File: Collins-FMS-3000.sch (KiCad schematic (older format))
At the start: 24 parts, among them U2 MCP23017_SO, U3 MCP23017_SO, U4 IS31FL3733B

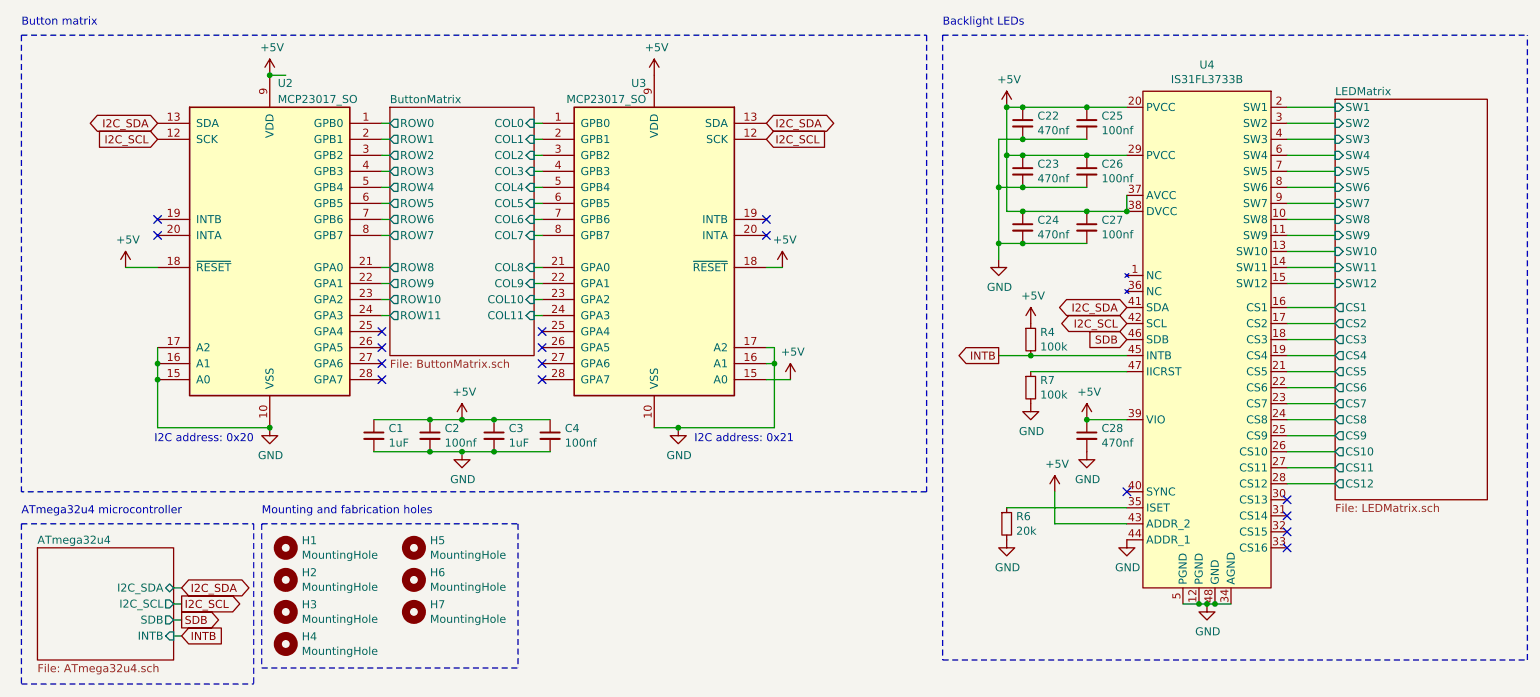
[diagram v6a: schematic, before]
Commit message: Remove diodes, update interrupt connections
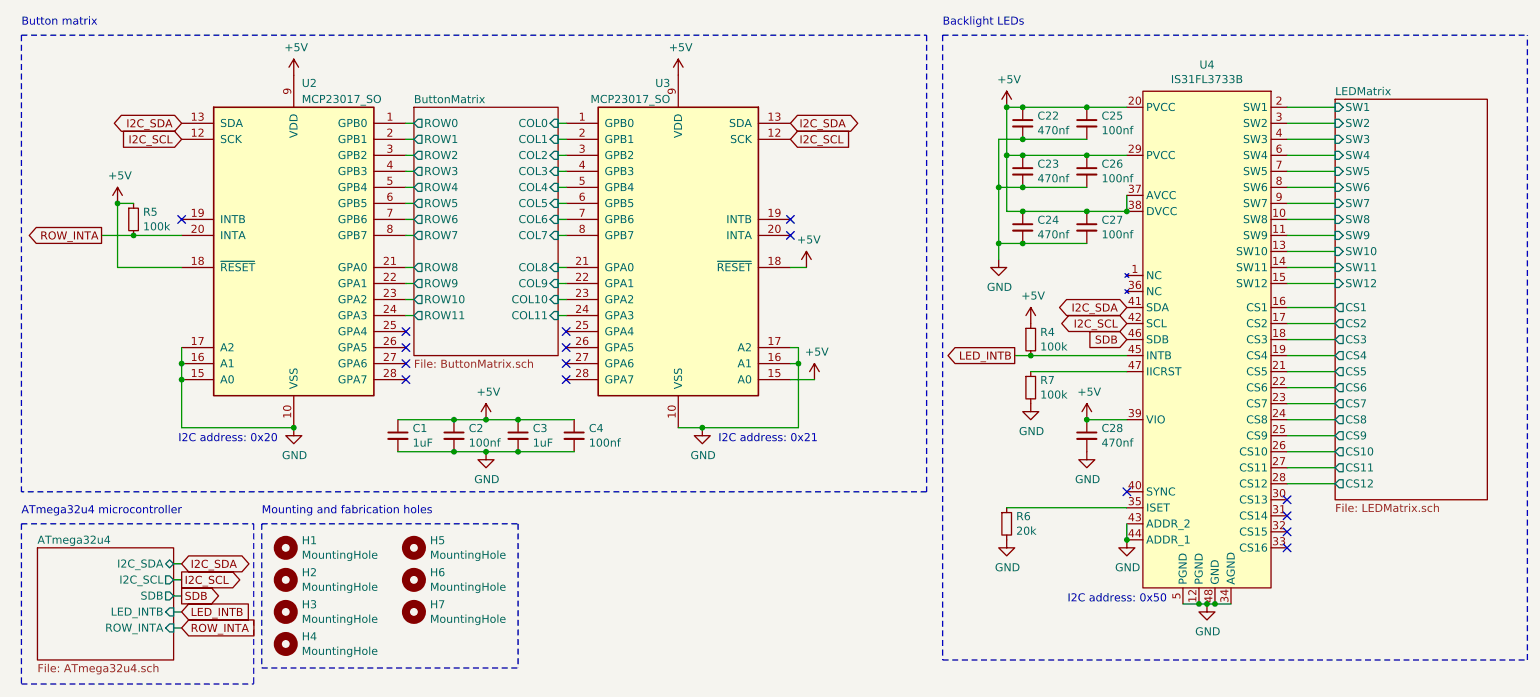
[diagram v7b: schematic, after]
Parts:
- added R5: 100k, Resistor_SMD:R_0402_1005Metric, symbol Device:R_Small
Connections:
- net +5V: now also R5.1; no longer U4.43 (ADDR_2)
- net GND: now also U4.43 (ADDR_2)
- net ROW_INTA: now reaches U2.20 (INTA)
- net ROW_INTA: now also R5.2
- net INTB renamed LED_INTB
- no-connect marks 17 -> 16
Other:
- note added: "I2C address: 0x50"
- moved on the sheet: C1, C2, C3, C4, U2, U3

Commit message: Connect unused pins
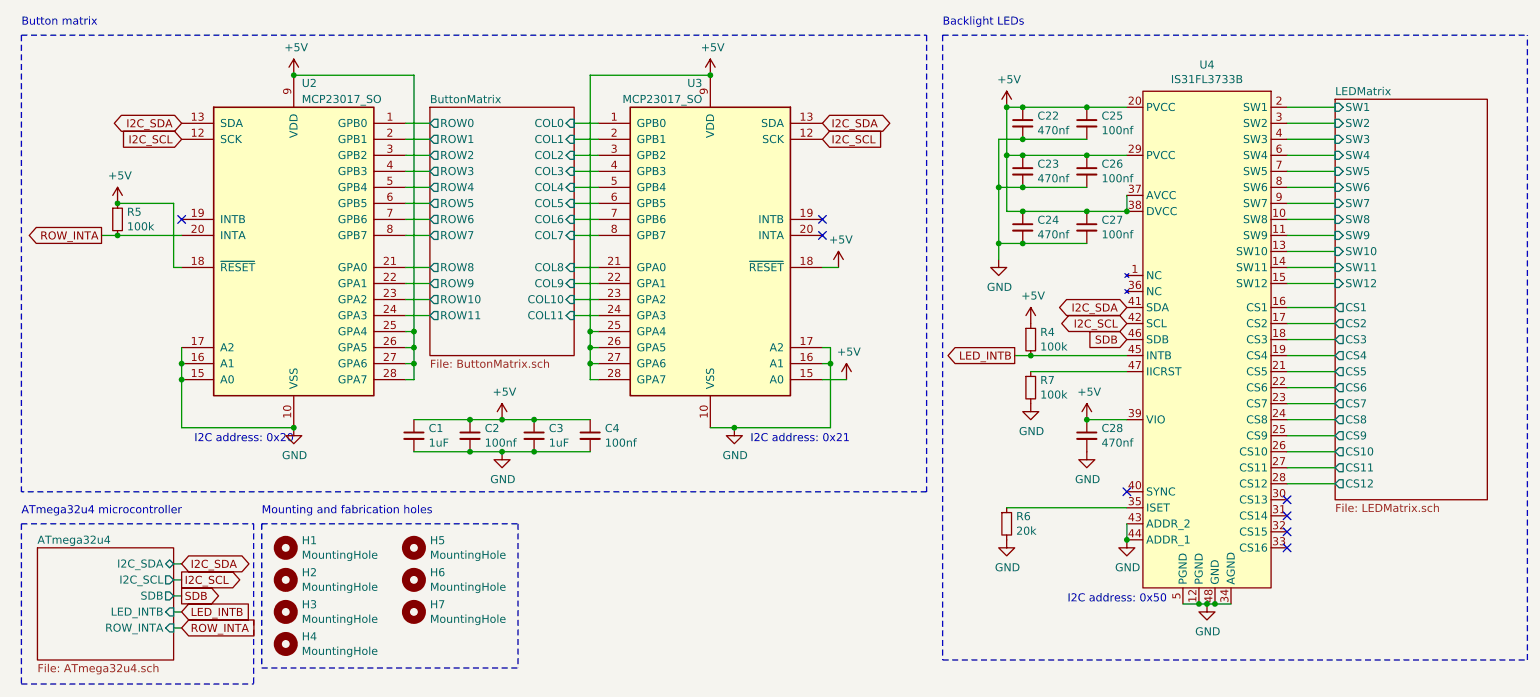
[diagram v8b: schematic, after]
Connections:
- net +5V: now also U2.25 (GPA4), U2.26 (GPA5), U2.27 (GPA6), U2.28 (GPA7), U3.25 (GPA4), U3.26 (GPA5), U3.27 (GPA6), U3.28 (GPA7)
- no-connect marks 16 -> 8
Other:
- moved on the sheet: C1, C2, C3, C4, R5, U3
